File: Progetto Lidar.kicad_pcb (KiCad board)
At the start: 2 copper layers, 130 x 77 mm, 33 parts, among them IC1 TLV74133PDBVR, IC2 LT1719IS6#TRPBF, J1 CONN_LASER, J10 Conn_01x08, J2 Conn_Coaxial, J3 Conn_02x18_Odd_Even, J4 Conn_01x10, J5 Conn_01x08, J6 Conn_01x08, J7 Conn_01x08, J8 Conn_SPI, J9 Conn_01x08, Y1 SiT2024BA-S2-33E-8.000000G

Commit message: Finito layout e schematico. Aggiornato Silkscreen
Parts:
- D1: value 5V_LED -> 5V
- D2: value 3V3_LED -> 3V3
- J2: value Conn_Coaxial -> CONN_RICEVITORE
- JP2: value SolderJumper_3_Open -> LDO_EN
- moved D1 22.3 mm to (181.9, 63.8), turned to 90 degrees
- moved D2 20.2 mm to (184.9, 63.8), turned to 90 degrees
- moved R3 18.1 mm to (187.2, 63.8), turned to -90 degrees
- moved R2 17.9 mm to (179.6, 63.8), turned to -90 degrees
- moved C8 11.7 mm to (198.6, 104.6), turned to 180 degrees
- moved C5 7.40 mm to (198.6, 102.4), turned to 180 degrees
- moved C1 5.80 mm to (181.3, 54.0)
- moved C2 5.80 mm to (185.3, 54.0)
- moved IC1 5.80 mm to (183.3, 57.1)
- moved JP1 5.80 mm to (180.5, 60.4)
- moved JP2 5.80 mm to (189.2, 57.1)
- moved IC_2 2.50 mm to (198.9, 107.2), turned to 0 degrees
- moved J1 0.26 mm to (205.5, 108.2)
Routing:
- net GND: track 324.1 -> 382.6 mm, vias 2 -> 9
- net /ARD_V_REF: track 6.89 -> 52.8 mm, vias 0 -> 1
- net +3V3: track 62.3 -> 92.9 mm
- net /TDC_START: track 22.4 -> 32.7 mm
- net /TDC_STOP: track 10.2 -> 20.0 mm
- net /RIC_STOP: track 0.00 -> 8.60 mm
- net +5V: track 198.9 -> 205.0 mm
- net /3V3_ARDUINO: track 89.9 -> 95.6 mm
- net /BUFFER_START: track 3.92 -> 7.53 mm
- net Net-(D2-Pad2): track 0.00 -> 3.05 mm
- net Net-(D1-Pad2): track 0.00 -> 3.05 mm
- net /ARD_BUFF_EN: track 32.6 -> 30.8 mm, vias 1 -> 0
- net /ARD_GPIO_53: track 10.6 -> 8.81 mm
- added copper zone on B.Cu, net GND
- added copper zone on F.Cu, net GND
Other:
- board text added: "+5V"
- board text added: "D22"
- board text added: "D23"
- board text added: "D24"
- board text added: "D25"
- board text added: "D26"
- board text added: "D27"
- board text added: "D28"
- board text added: "D29"
- board text added: "D30"
- board text added: "D31"
- board text added: "D32"
- board text added: "D33"
- board text added: "D34"
- board text added: "D35"
- board text added: "D36"
- board text added: "D37"
- board text added: "D38"
- board text added: "D39"
- board text added: "D40"
- board text added: "D41"
- board text added: "D42"
- board text added: "D43"
- board text added: "D44"
- board text added: "D45"
- board text added: "D46"
- board text added: "D47"
- board text added: "D48"
- board text added: "D49"
- board text added: "D50"
- board text added: "D51"
- board text added: "D52"
- board text added: "D53"
- board text added: "GND"
- board text added: "V1.1 25/03/2025"
- board text removed: "V1.0 19/03/2025"

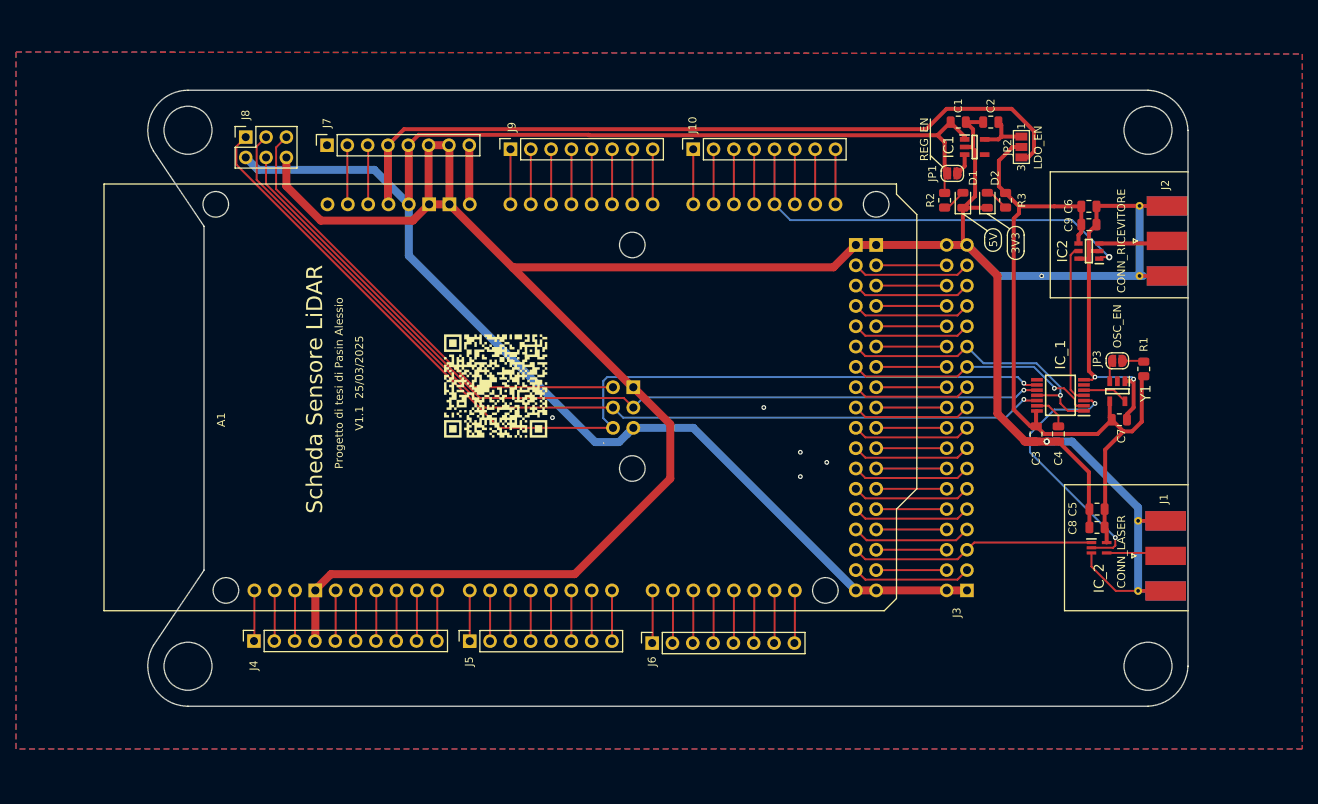
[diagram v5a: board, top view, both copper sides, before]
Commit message: Aggiunto pinou di Arduino su silkscreen
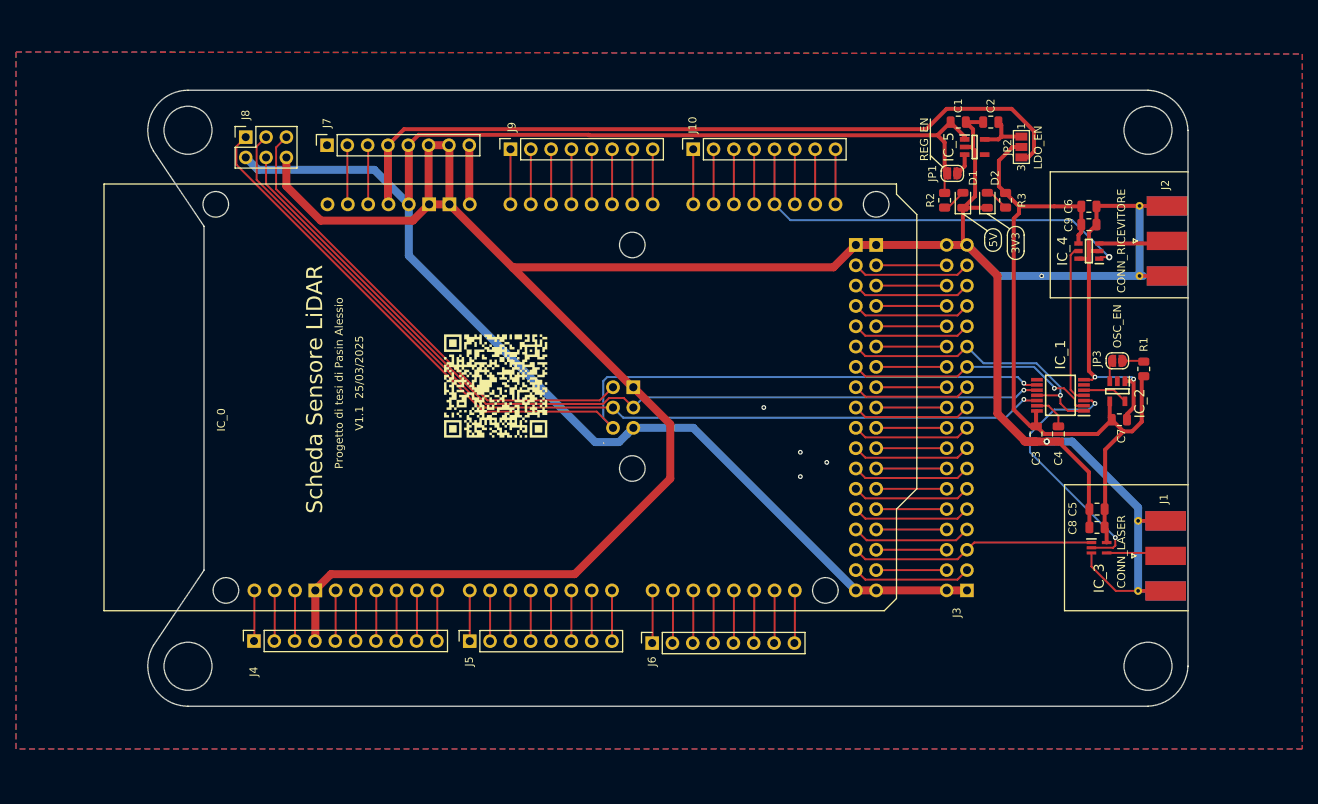
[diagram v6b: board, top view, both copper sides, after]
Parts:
- renumbered A1 to IC_0, Y1 to IC_2, IC_2 to IC_3, IC2 to IC_4, IC1 to IC_5
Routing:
- net /SPI_RESET: track 59.4 -> 60.8 mm
- net /SPI_MOSI: track 112.2 -> 112.8 mm
- net GND: vias 9 -> 8
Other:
- board text added: "3V3"
- board text added: "5V"
- board text added: "A0"
- board text added: "A1"
- board text added: "A10"
- board text added: "A11"
- board text added: "A2"
- board text added: "A3"
- board text added: "A4"
- board text added: "A5"
- board text added: "A6"
- board text added: "A7"
- board text added: "A8"
- board text added: "A9"
- board text added: "AREF"
- board text added: "CANR"
- board text added: "CANT"
- board text added: "D0"
- board text added: "D1"
- board text added: "D10"
- board text added: "D11"
- board text added: "D12"
- board text added: "D13"
- board text added: "D14"
- board text added: "D15"
- board text added: "D16"
- board text added: "D17"
- board text added: "D18"
- board text added: "D19"
- board text added: "D2"
- board text added: "D20"
- board text added: "D21"
- board text added: "D3"
- board text added: "D4"
- board text added: "D5"
- board text added: "D6"
- board text added: "D7"
- board text added: "D8"
- board text added: "D9"
- board text added: "DAC0"
- board text added: "DAC1"
- board text added: "IORF"
- board text added: "MISO"
- board text added: "MOSI"
- board text added: "RST1"
- board text added: "RST2"
- board text added: "SCK"
- board text added: "SCL1"
- board text added: "SDA1"
- board text added: "VIN"
- board text added: "X"

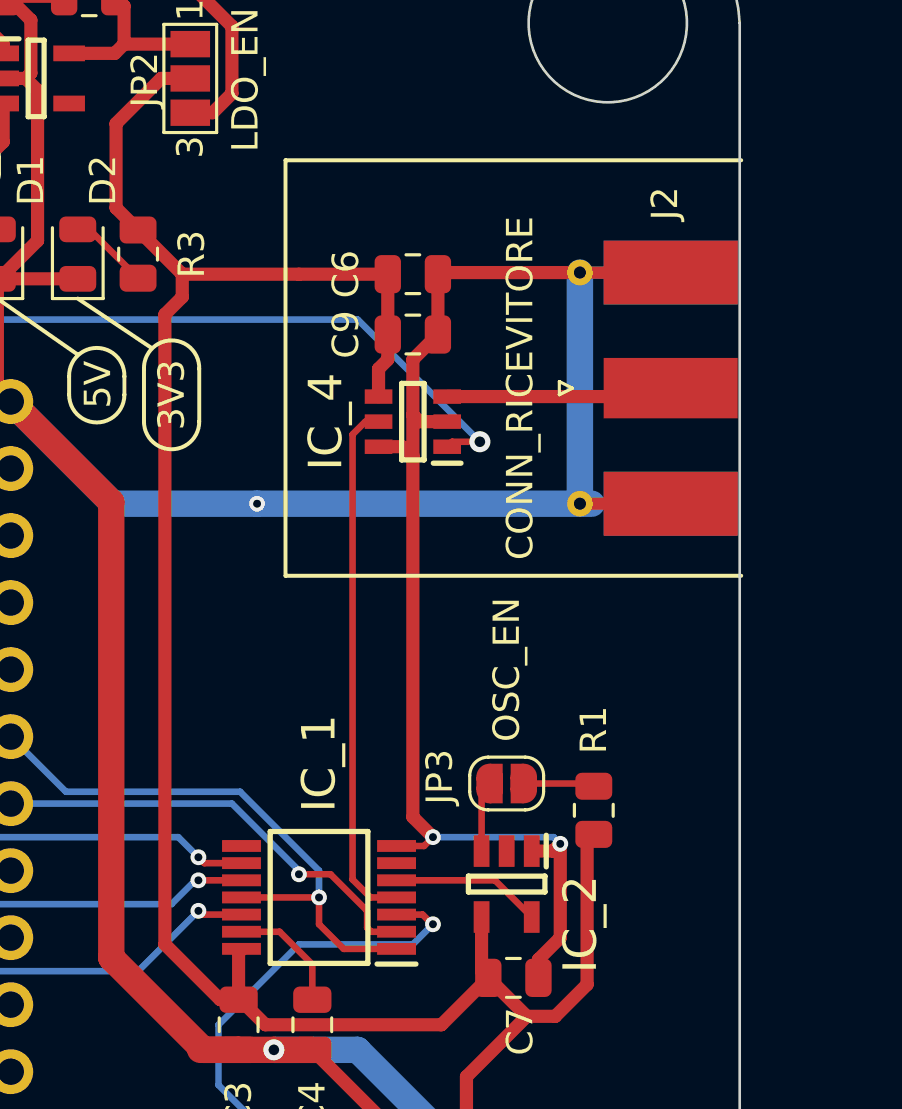
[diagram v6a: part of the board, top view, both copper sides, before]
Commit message: Corretto simulazione, aggiunto circuito di condizionamento del segnale e modificato il layout
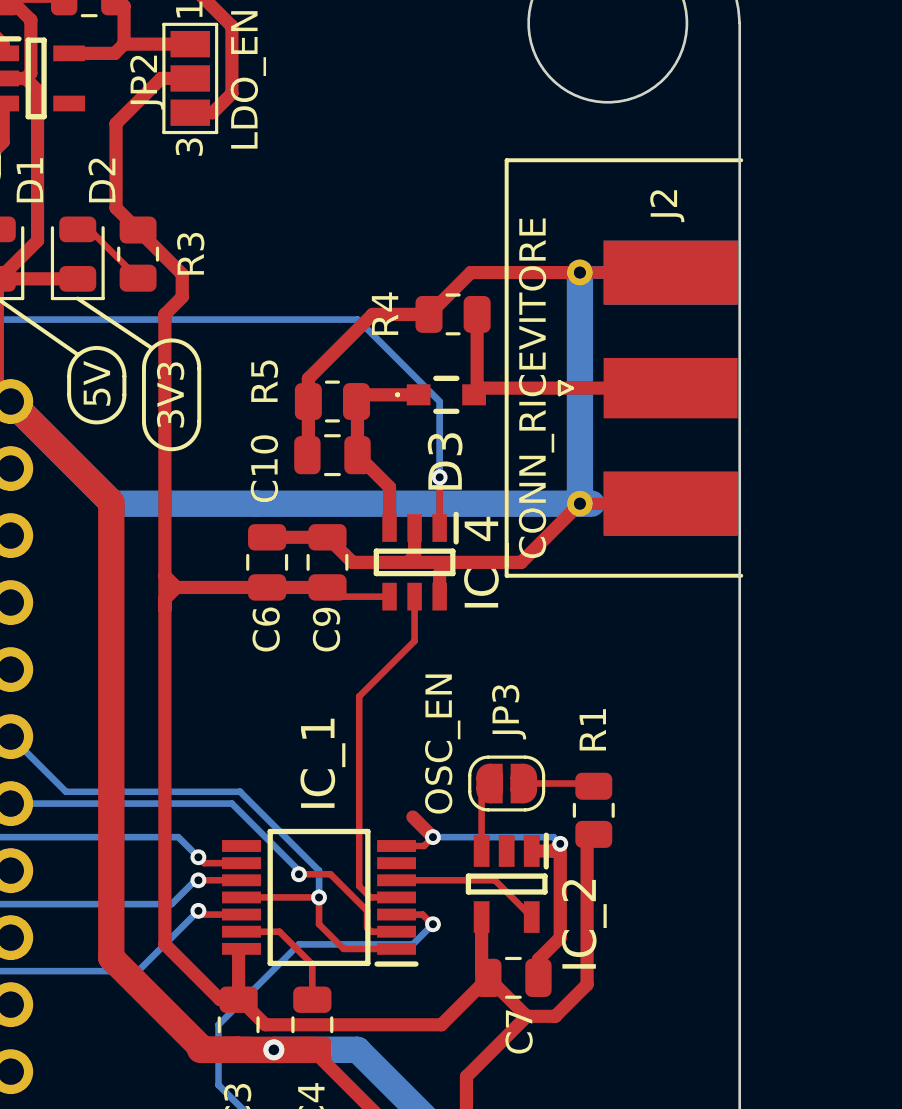
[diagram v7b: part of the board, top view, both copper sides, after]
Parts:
- added C10: 50pF, Capacitor_SMD:C_0805_2012Metric, F.Cu at (194.6, 71.4)
- added D3: D_Shockley, Libreria_componenti_footprint:RB511VM30TE17, F.Cu at (198.9, 69.1)
- added R4: 47, Resistor_SMD:R_0805_2012Metric, F.Cu at (199.1, 66.0)
- added R5: 180, Resistor_SMD:R_0805_2012Metric, F.Cu at (194.6, 69.3)
- moved C6 12.2 mm to (192.1, 75.4), turned to 90 degrees
- moved C9 9.22 mm to (194.4, 75.4), turned to 90 degrees
- moved IC_4 5.33 mm to (197.7, 75.4), turned to -90 degrees
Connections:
- IC_4 pad 3: /RIC_STOP -> Net-(IC_4-Pad3)
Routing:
- net Net-(IC_4-Pad3): track 0.00 -> 7.78 mm
- net /TDC_STOP: track 20.0 -> 13.4 mm
- net +3V3: track 92.9 -> 90.2 mm
- net /RIC_STOP: track 8.60 -> 10.7 mm
- net GND: track 382.6 -> 384.2 mm, vias 8 -> 7
- net /ARD_V_REF: track 52.8 -> 54.1 mm

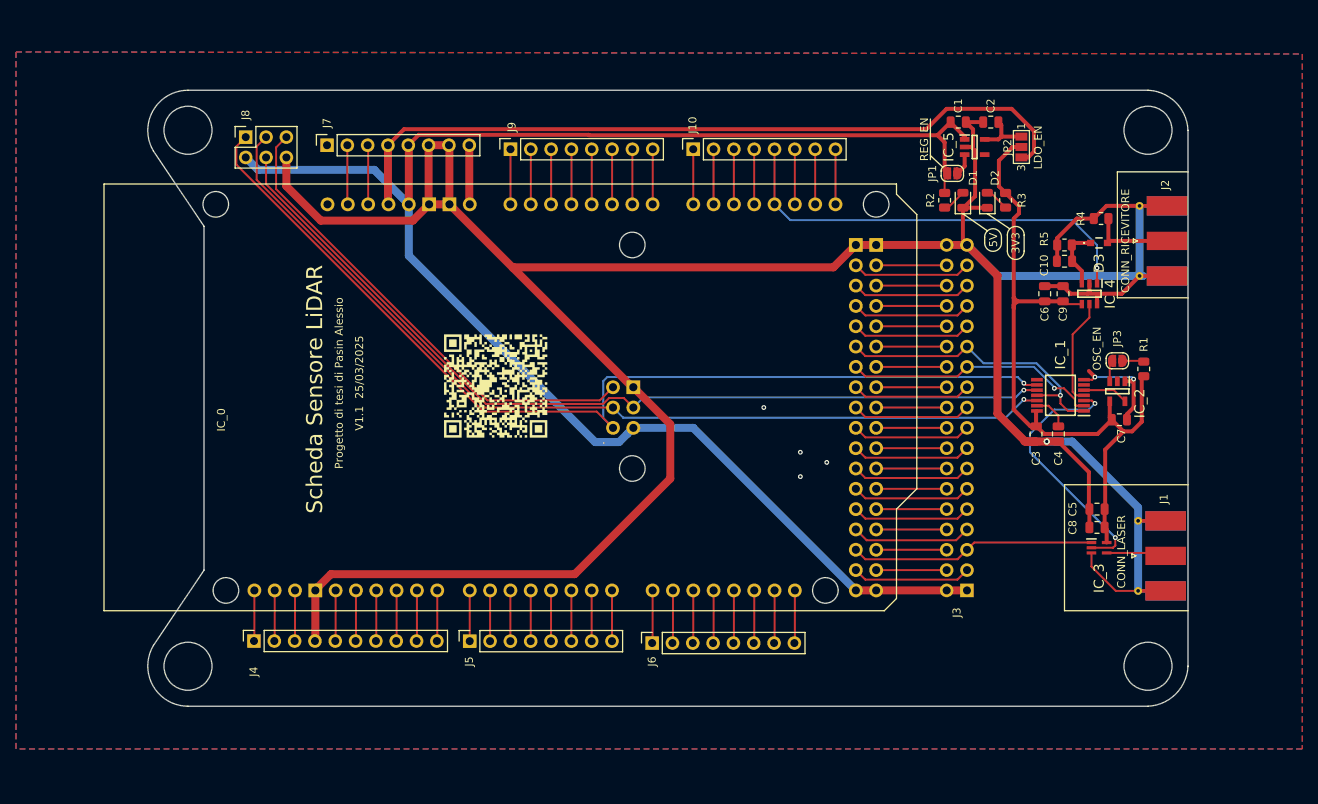
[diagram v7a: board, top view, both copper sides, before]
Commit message: Sistemato alcuni errori di circuito, aggiunto resistenze per SPI, aggiunto condensatori di filtraggio
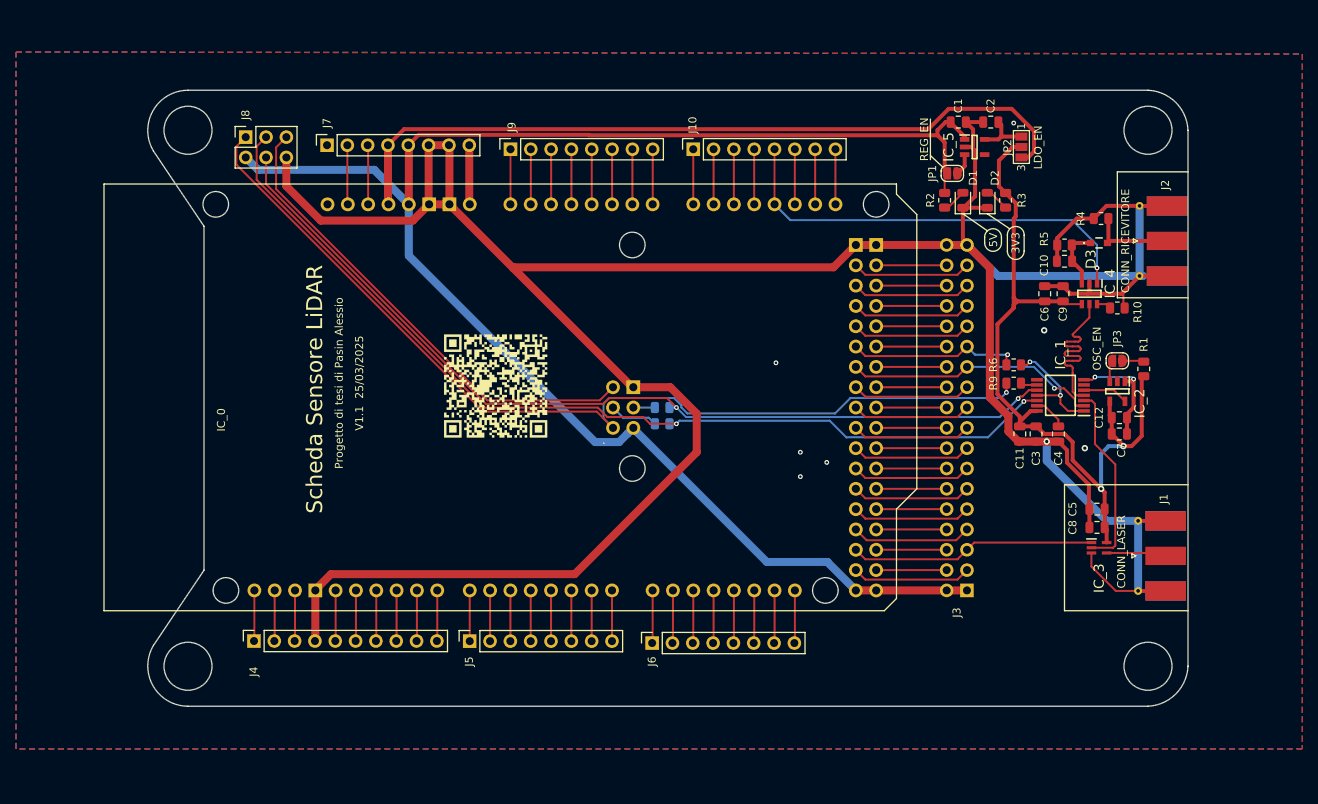
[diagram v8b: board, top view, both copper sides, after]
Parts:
- added C11: 1nF, Capacitor_SMD:C_0805_2012Metric, F.Cu at (189.0, 93.0)
- added C12: 1nF, Capacitor_SMD:C_0805_2012Metric, F.Cu at (201.4, 90.9)
- added R10: 100, Resistor_SMD:R_0805_2012Metric, F.Cu at (201.2, 77.2)
- added R6: 100, Resistor_SMD:R_0805_2012Metric, F.Cu at (188.2, 84.3)
- added R7: 100, Resistor_SMD:R_0805_2012Metric, B.Cu at (144.3, 89.7)
- added R8: 100, Resistor_SMD:R_0805_2012Metric, B.Cu at (144.3, 91.7)
- added R9: 100, Resistor_SMD:R_0805_2012Metric, F.Cu at (188.2, 86.6)
- moved C7 1.78 mm to (201.4, 93.0)
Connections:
- IC_0 pad D44: /SPI_CS -> /ARD_GPIO_44
- IC_0 pad MOSI: /SPI_MOSI -> Net-(IC_0-PadMOSI)
- IC_0 pad SCK: /SPI_SCK -> Net-(IC_0-PadSCK)
- IC_1 pad 9: /SPI_MISO -> Net-(IC_1-Pad9)
- IC_4 pad 6: GND -> Net-(IC_4-Pad6)
- J3 pad 25: /SPI_CS -> /ARD_GPIO_44
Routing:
- net /SPI_CS: track 37.0 -> 14.7 mm, vias 1 -> 2
- net /ARD_GPIO_44: track 0.00 -> 21.7 mm, vias 0 -> 1
- net /TDC_STOP: track 13.4 -> 23.5 mm
- net /TDC_START: track 32.7 -> 23.4 mm, vias 2 -> 0
- net +3V3: track 90.2 -> 99.0 mm, vias 0 -> 2
- net GND: track 384.2 -> 390.7 mm, vias 7 -> 10
- net Net-(IC_0-PadSCK): track 0.00 -> 6.07 mm
- net /SPI_MISO: track 125.8 -> 122.0 mm
- net /SPI_SCK: track 116.7 -> 119.8 mm, vias 1 -> 2
- net Net-(IC_0-PadMOSI): track 0.00 -> 2.69 mm
- net Net-(IC_1-Pad9): track 0.00 -> 2.08 mm
- net /SPI_MOSI: track 112.8 -> 114.6 mm, vias 1 -> 2
- net Net-(IC_4-Pad6): track 0.00 -> 1.83 mm
